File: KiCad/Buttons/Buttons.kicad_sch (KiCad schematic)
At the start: 0 parts

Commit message: fixed power board, replaced sketchy voltage divider - op amp cct. with an LDO to product +5V
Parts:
- added J1: 691137710003, Header 691137710003:691137710003, symbol Header 691137710003:691137710003
- added J2: 691137710002, Header 691137710002:691137710002, symbol Header 691137710002:691137710002
- added R1, R2, R3: 30k, Resistor_SMD:R_0603_1608Metric, symbol Device:R_US
- added SW1, SW2, SW3: D6R90F2LFS, Switch Push Button D6R90F2LFS:D6R90_CNK, symbol Switch Push Button D6R90F2LFS:D6R90F2LFS
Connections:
- new net +5V: J2.1, SW1.1, SW1.4, SW2.1, SW2.4, SW3.1, SW3.4
- new net GND: J2.2, R1.2, R2.2, R3.2
- new net Out 1: J1.1, R1.1, SW1.2, SW1.3
- new net Out 2: J1.2, R2.1, SW2.2, SW2.3
- new net Out3: J1.3, R3.1, SW3.2, SW3.3

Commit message: added test points
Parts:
- added TP? (x6): TestPoint_Small, symbol Connector:TestPoint_Small
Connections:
- net +5V: now also TP?.1, TP?.1, TP?.1
- net Out 1: now also TP?.1
- net Out 2: now also TP?.1
- net Out3: now also TP?.1
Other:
- moved on the sheet: J1, J2, R1, R2, R3, SW1, SW2, SW3

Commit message: added power indicator LEDs
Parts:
- added D1: LED, symbol Device:LED
- added R4: R_US, symbol Device:R_US
- gave numbers to parts that had none: 6
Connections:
- net +5V: now also D1.2 (A)
- net GND: now also R4.2
- new net: D1.1 (K), R4.1

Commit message: added mounting holes to schematics, adjusted board sizes
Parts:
- added H1, H2, H3, H4: MountingHole, MountingHole:MountingHole_3.2mm_M3, symbol Mechanical:MountingHole

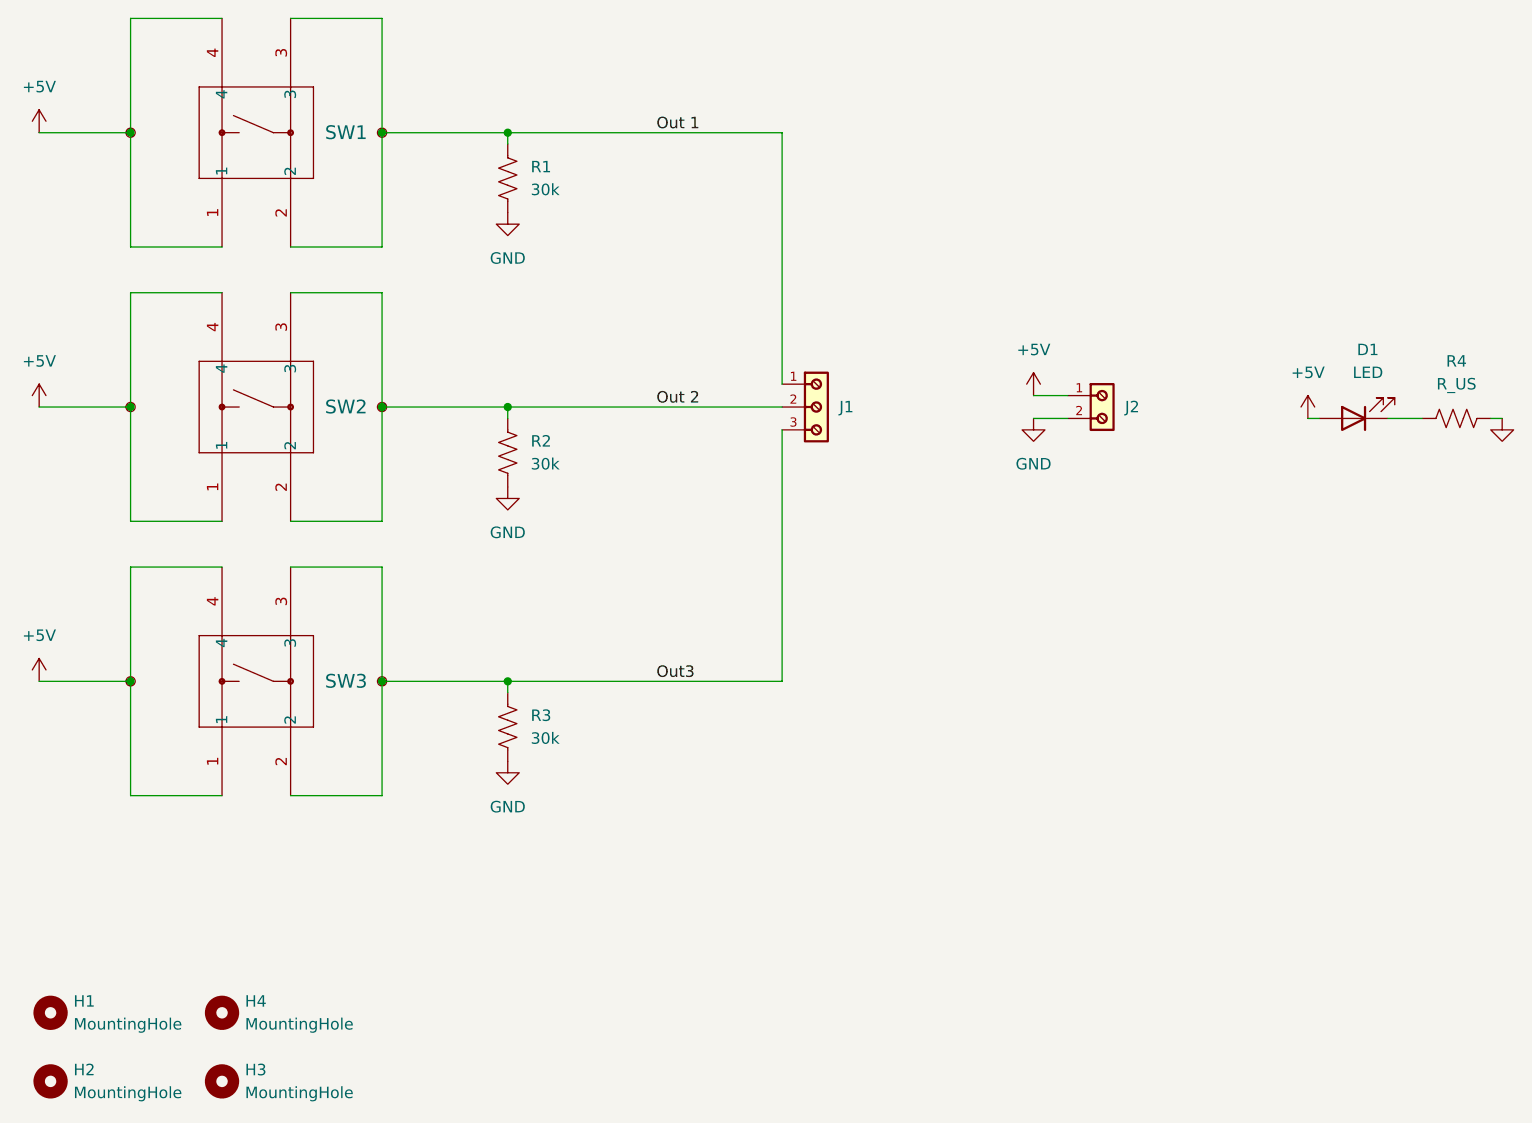
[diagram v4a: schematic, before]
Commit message: buttons pcb layout done
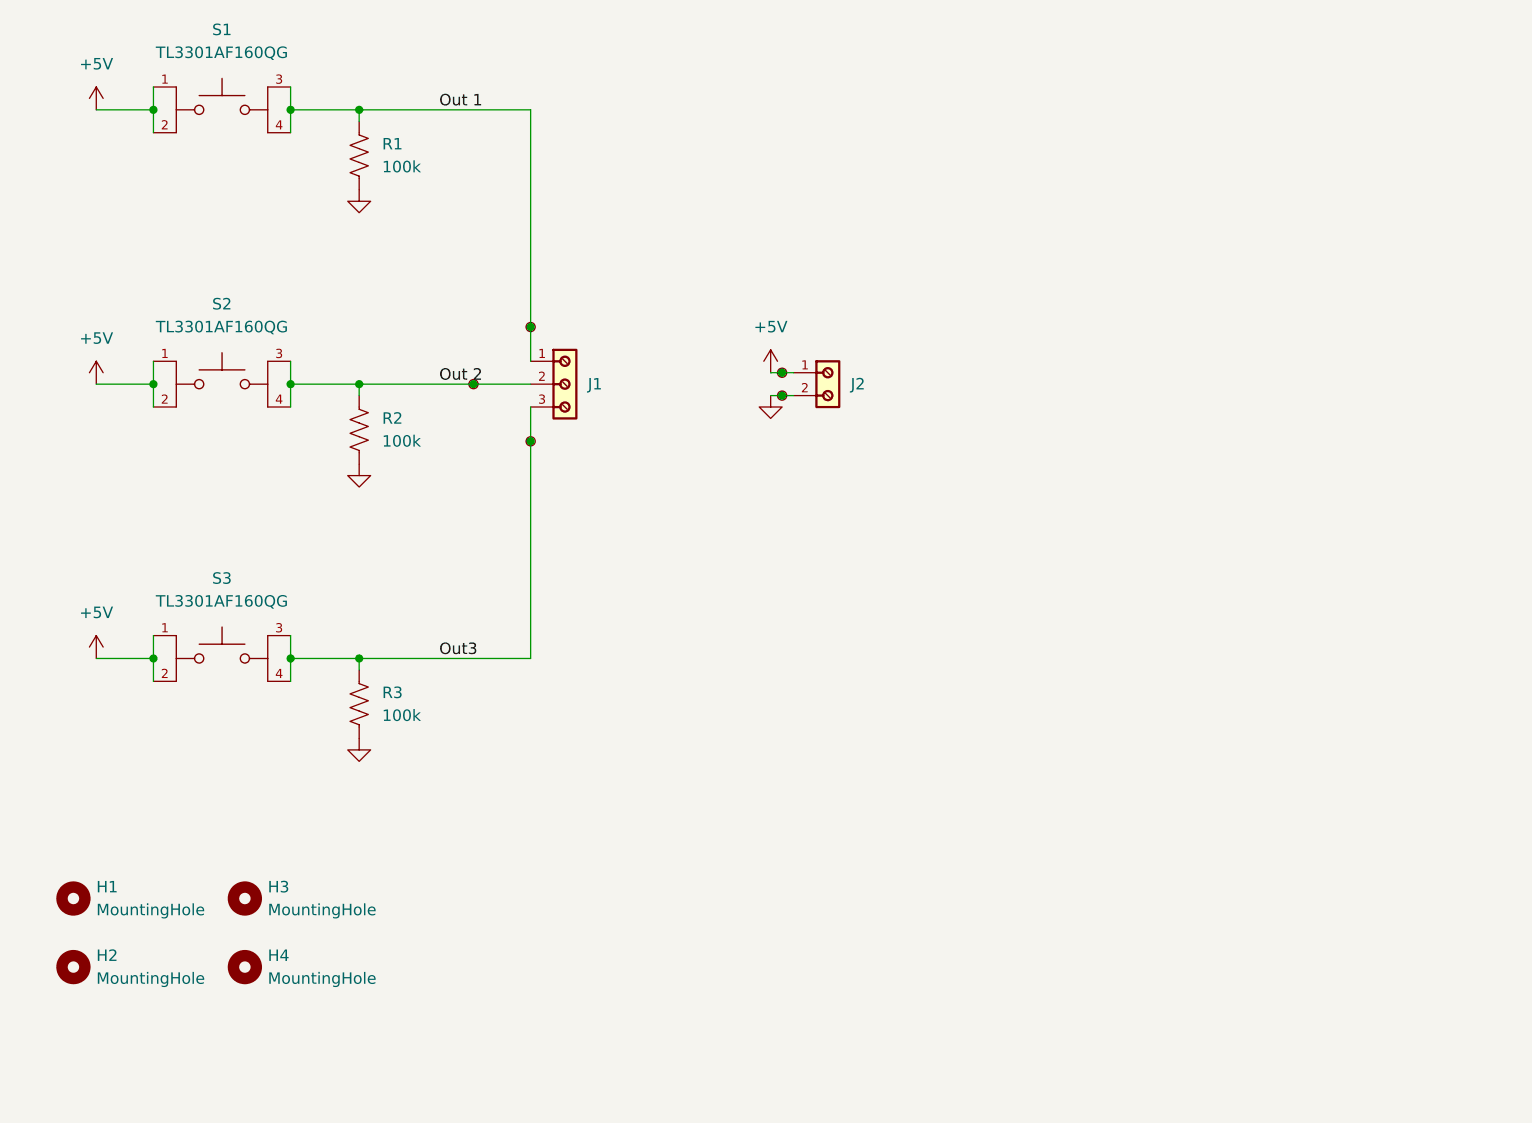
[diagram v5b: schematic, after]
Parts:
- removed D1: LED, symbol Device:LED
- removed R4: R_US, symbol Device:R_US
- removed SW1, SW2, SW3: D6R90F2LFS, Switch Push Button D6R90F2LFS:D6R90_CNK, symbol Switch Push Button D6R90F2LFS:D6R90F2LFS
- removed TP2, TP3: TestPoint_Small, symbol Connector:TestPoint_Small
- added S1, S2, S3: TL3301AF160QG, TL3301AF160QG:SW_TL3301AF160QG, symbol TL3301AF160QG:TL3301AF160QG
- added TP7: TestPoint_Small, TestPoint:TestPoint_Keystone_5000-5004_Miniature, symbol Connector:TestPoint_Small
- R1, R2, R3: value 30k -> 100k; footprint Resistor_SMD:R_0603_1608Metric -> Resistor_SMD:R_0805_2012Metric
- TP1, TP4, TP5, TP6: footprint (none) -> TestPoint:TestPoint_Keystone_5000-5004_Miniature
- renumbered H4 to H3, H3 to H4
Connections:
- net +5V: now also S1.1, S1.2, S2.1, S2.2, S3.1, S3.2
- net GND: now also TP7.1
- net Out 1: now also S1.3, S1.4
- net Out 2: now also S2.3, S2.4
- net Out3: now also S3.3, S3.4
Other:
- moved on the sheet: H1, H2, H3, H4, J1, J2, R1, R2, R3

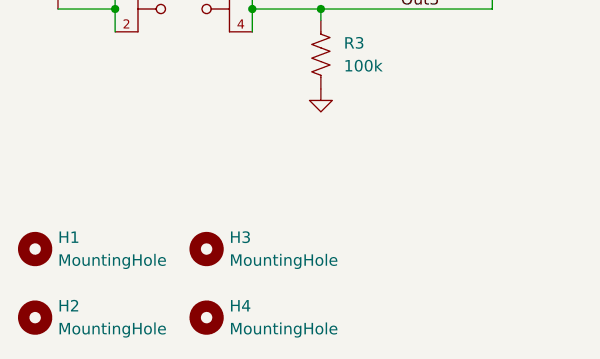
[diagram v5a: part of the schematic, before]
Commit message: changed buttons pcb layout to be smaller
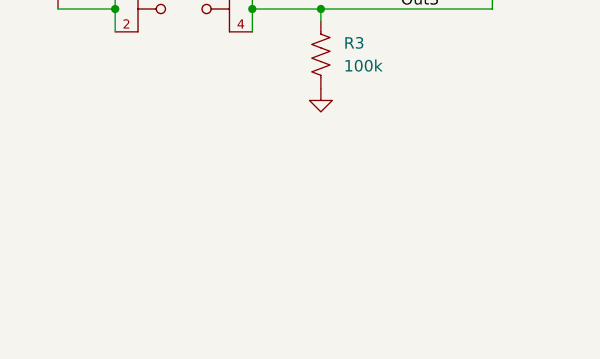
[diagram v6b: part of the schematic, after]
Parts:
- removed H1, H2, H3, H4: MountingHole, MountingHole:MountingHole_3.2mm_M3, symbol Mechanical:MountingHole

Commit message: preparation to merge project back into one board
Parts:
- R1, R2, R3: KiLib_Generator (none) -> SMD_2terminal_chip_molded
- renumbered TP7 to TP1, TP1 to TP2, TP4 to TP3, TP5 to TP4, TP6 to TP5
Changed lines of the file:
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@@
 		(dnp no)
 		(fields_autoplaced yes)
-		(property "Reference" "TP5"
+		(property "Reference" "TP4"
 			(at 68.58 59.6899 0)
 			(hide yes)
@@
 			(project "Buttons"
 				(path "/13047048-817a-4b05-9170-e5cf0f7134f2"
-					(reference "TP5")
+					(reference "TP4")
 					(unit 1)
 				)
@@
 			)
 		)
+		(property "KiLib_Generator" "SMD_2terminal_chip_molded"
+			(at 54.61 96.52 0)
+			(hide yes)
+			(show_name no)
+			(do_not_autoplace no)
+			(effects
+				(font
+					(size 1.27 1.27)
+				)
+			)
+		)
 		(pin "1"
 		)
@@
 			)
 		)
+		(property "KiLib_Generator" "SMD_2terminal_chip_molded"
+			(at 54.61 66.04 0)
+			(hide yes)
+			(show_name no)
+			(do_not_autoplace no)
+			(effects
+				(font
+					(size 1.27 1.27)
+				)
+			)
+		)
 		(pin "1"
 		)
@@
 			)
 		)
+		(property "KiLib_Generator" "SMD_2terminal_chip_molded"
+			(at 54.61 35.56 0)
+			(hide yes)
+			(show_name no)
+			(do_not_autoplace no)
+			(effects
+				(font
+					(size 1.27 1.27)
+				)
+			)
+		)
 		(pin "1"
 		)
@@
 		(dnp no)
 		(fields_autoplaced yes)
-		(property "Reference" "TP6"
+		(property "Reference" "TP5"
 			(at 74.93 66.0399 0)
 			(hide yes)
@@
 			(project "Buttons"
 				(path "/13047048-817a-4b05-9170-e5cf0f7134f2"
-					(reference "TP6")
+					(reference "TP5")
 					(unit 1)
 				)
@@
 		(dnp no)
 		(fields_autoplaced yes)
-		(property "Reference" "TP7"
+		(property "Reference" "TP1"
 			(at 102.87 60.9599 0)
 			(hide yes)
@@
 			(project "Buttons"
 				(path "/13047048-817a-4b05-9170-e5cf0f7134f2"
-					(reference "TP7")
+					(reference "TP1")
 					(unit 1)
 				)
@@
 		(dnp no)
 		(fields_autoplaced yes)
-		(property "Reference" "TP4"
+		(property "Reference" "TP3"
 			(at 74.93 53.3399 0)
 			(hide yes)
@@
 			(project "Buttons"
 				(path "/13047048-817a-4b05-9170-e5cf0f7134f2"
-					(reference "TP4")
+					(reference "TP3")
 					(unit 1)
 				)
@@
 		(dnp no)
 		(fields_autoplaced yes)
-		(property "Reference" "TP1"
+		(property "Reference" "TP2"
 			(at 102.87 58.4199 0)
 			(hide yes)
@@
 			(project "Buttons"
 				(path "/13047048-817a-4b05-9170-e5cf0f7134f2"
-					(reference "TP1")
-					(unit 1)
-				)
+					(reference "TP2")
+					(unit 1)
+				)

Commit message: made all components THT on the buttons board
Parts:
- R1, R2, R3: footprint Resistor_SMD:R_0805_2012Metric -> Resistor_THT:R_Axial_DIN0207_L6.3mm_D2.5mm_P7.62mm_Horizontal
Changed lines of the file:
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@@
 			)
 		)
-		(property "Footprint" "Resistor_SMD:R_0805_2012Metric"
+		(property "Footprint" "Resistor_THT:R_Axial_DIN0207_L6.3mm_D2.5mm_P7.62mm_Horizontal"
 			(at 55.626 96.774 90)
 			(hide yes)
@@
 			)
 		)
-		(property "Footprint" "Resistor_SMD:R_0805_2012Metric"
+		(property "Footprint" "Resistor_THT:R_Axial_DIN0207_L6.3mm_D2.5mm_P7.62mm_Horizontal"
 			(at 55.626 66.294 90)
 			(hide yes)
@@
 			)
 		)
-		(property "Footprint" "Resistor_SMD:R_0805_2012Metric"
+		(property "Footprint" "Resistor_THT:R_Axial_DIN0207_L6.3mm_D2.5mm_P7.62mm_Horizontal"
 			(at 55.626 35.814 90)
 			(hide yes)
